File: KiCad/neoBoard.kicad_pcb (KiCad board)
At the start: 2 copper layers, 40 x 40 mm, 74 parts, among them J1 SW, J10 CONN_01X04_Straight, J11 CONN_01X04_Straight, J12 CONN_01X04_Straight, J13 CONN_01X04_Straight, J2 μUSB, J3 BATT, J6 CONN_01X12_Straight, J7 CONN_02X12_Straight, J8 CONN_01X04_Straight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

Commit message: PCB updated
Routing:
- net GND: track 137.4 -> 285.6 mm, vias 116 -> 108
- net /MOTEN: track 18.2 -> 24.9 mm, vias 2 -> 4
- net 3.3V: track 113.0 -> 110.4 mm, vias 7 -> 9
- net 5V: track 159.6 -> 157.9 mm
- net Net-(C5-Pad1): track 19.2 -> 17.8 mm
- net Net-(Q1-Pad1): track 4.76 -> 3.71 mm, vias 2 -> 0

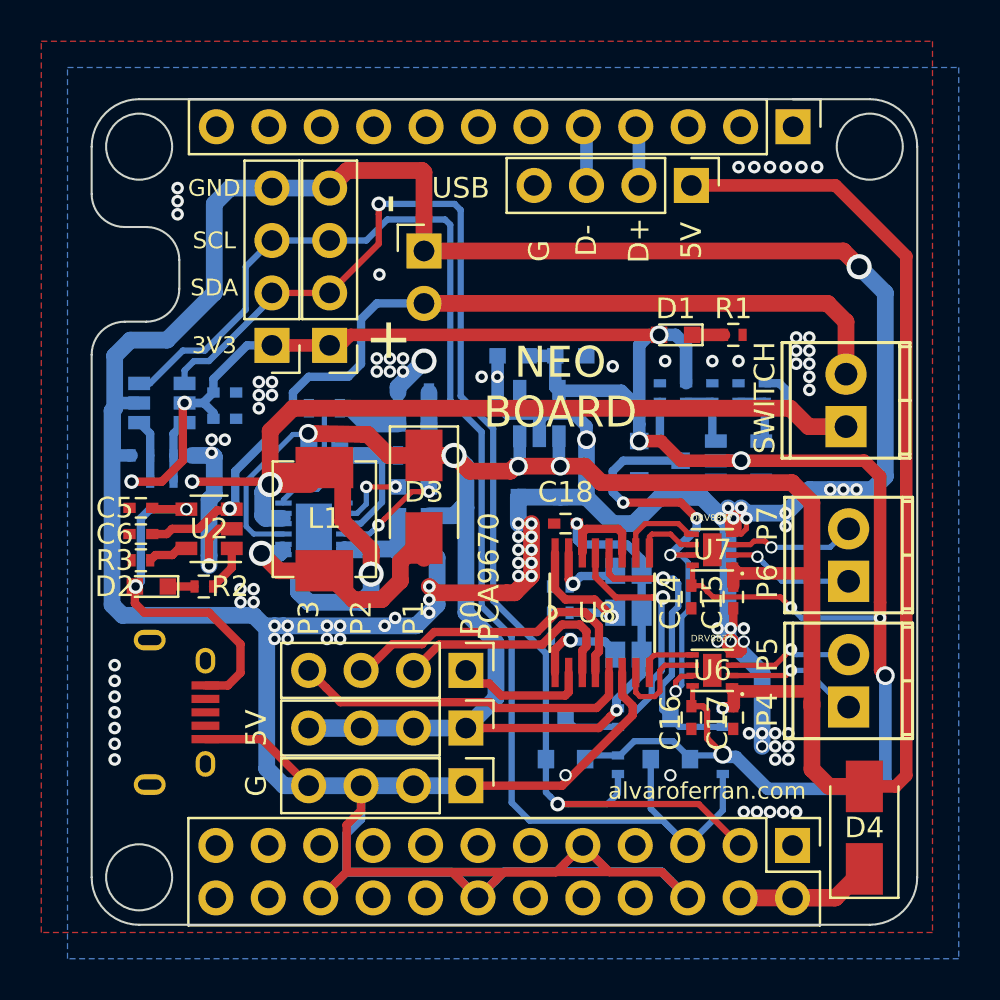
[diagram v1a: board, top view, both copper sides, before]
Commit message: Improved GND connections
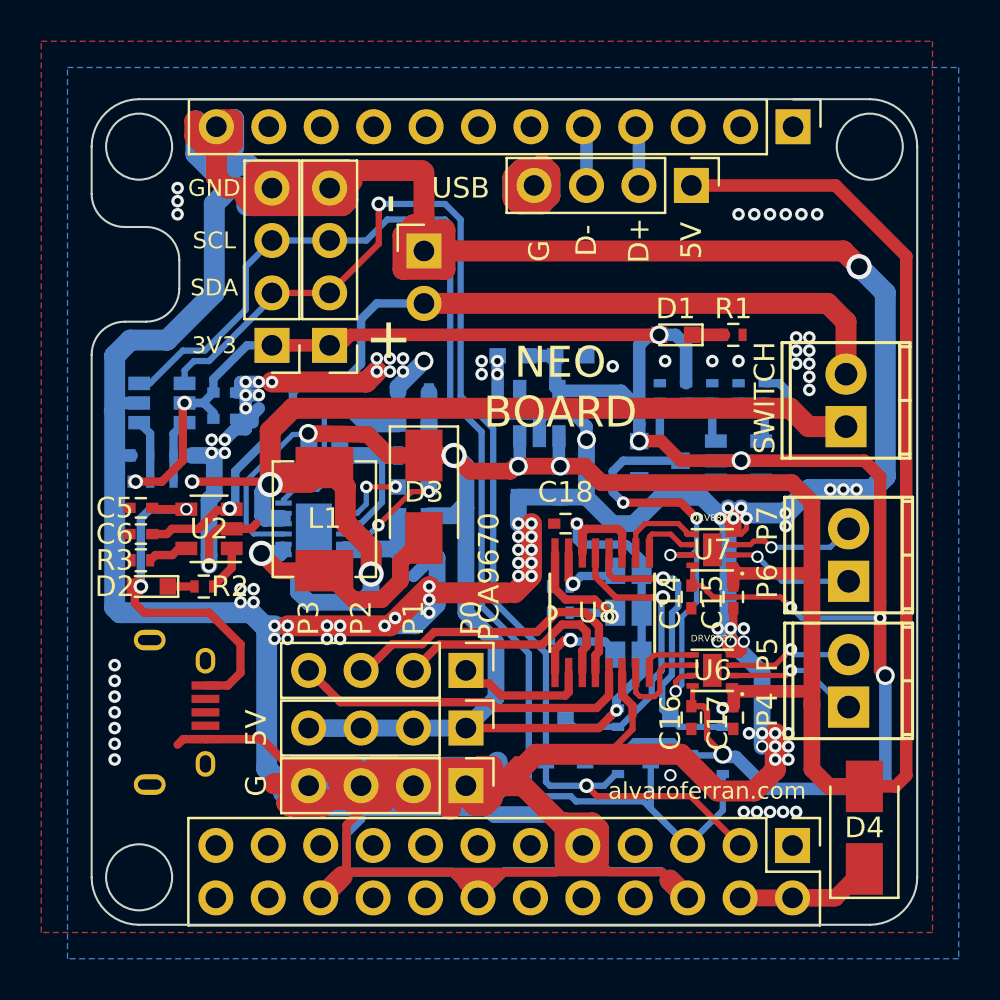
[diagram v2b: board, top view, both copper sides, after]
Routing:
- net GND: track 285.6 -> 502.5 mm, vias 108 -> 110
- net /SDA: track 63.6 -> 60.7 mm
- net Net-(D3-Pad2): track 13.2 -> 12.2 mm
- net /MOTEN: track 24.9 -> 25.8 mm
- net /SCL: track 67.4 -> 66.6 mm
- net VBAT: track 59.5 -> 60.2 mm
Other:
- net class Default: clearance 0 -> 0.0254
- rule trace_clearance: 0 -> 0.0254
- rule trace_min: 0.1524 -> 0.0254

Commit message: Change PCA9670 to PCA9685
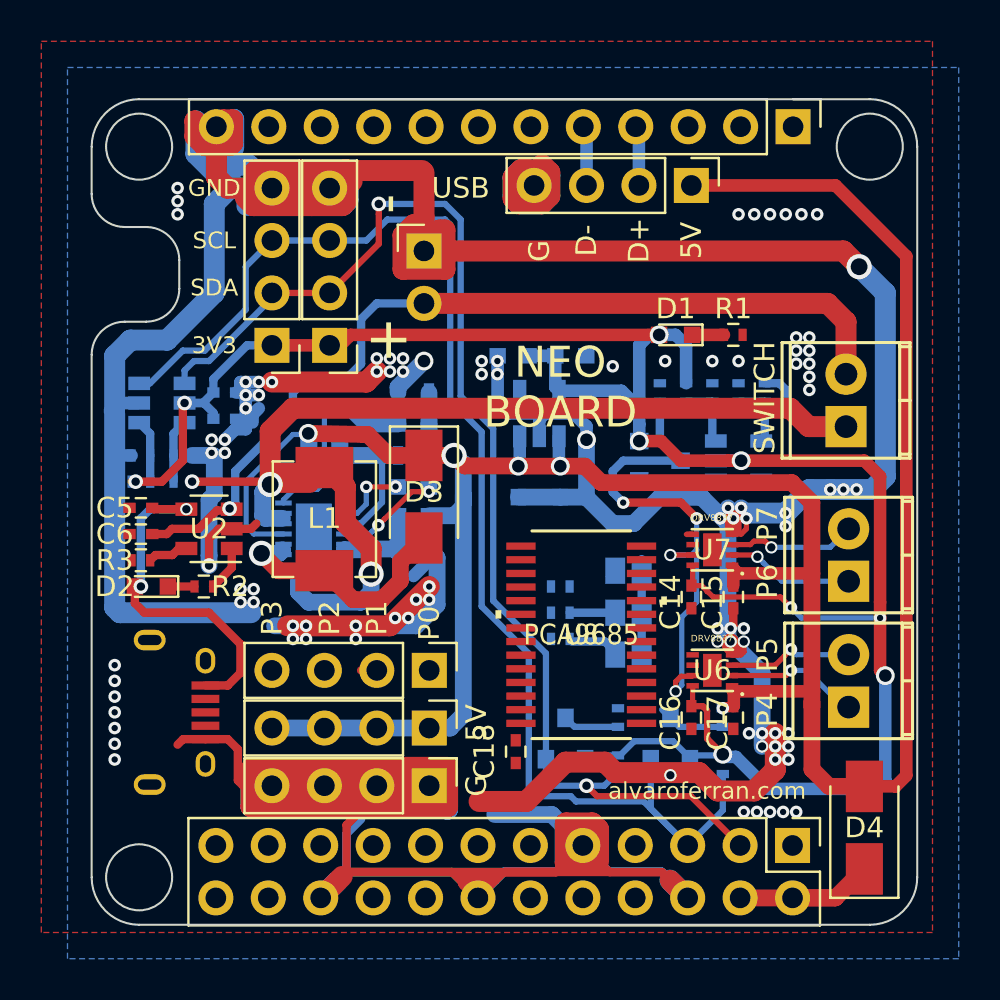
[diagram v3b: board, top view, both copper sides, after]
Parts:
- U8: value PCA9670 -> PCA9685; footprint alvaroferran:TSSOP-16 -> alvaroferran:TSSOP-28
- moved C18 11.3 mm to (169.0, 96.6), turned to 270 degrees
- moved J11 1.78 mm to (164.8, 98.3)
- moved J12 1.78 mm to (164.8, 95.5)
- moved J13 1.78 mm to (164.8, 92.7)
- moved U8 1.47 mm to (172.2, 91.0), turned to 180 degrees
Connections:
- U8 pad 1: Net-(JP3-Pad1) -> Net-(JP1-Pad1)
- U8 pad 10: /MOT2B -> /MOT1A
- U8 pad 11: 5V -> /MOT1B
- U8 pad 12: /SCLH -> /MOT2A
- U8 pad 13: /SDAH -> /MOT2B
- U8 pad 14: 5V -> GND
- U8 pad 15: Net-(JP1-Pad1) -> Net-(U8-Pad15)
- U8 pad 16: Net-(JP2-Pad1) -> Net-(U8-Pad16)
- U8 pad 2: /GPIO0 -> Net-(JP2-Pad1)
- U8 pad 3: /GPIO1 -> Net-(JP3-Pad1)
- U8 pad 4: /GPIO2 -> GND
- U8 pad 5: /GPIO3 -> GND
- U8 pad 6: GND -> /GPIO0
- U8 pad 7: /MOT1A -> /GPIO1
- U8 pad 8: /MOT1B -> /GPIO2
- U8 pad 9: /MOT2A -> /GPIO3
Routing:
- net GND: track 502.5 -> 443.6 mm, vias 110 -> 98
- net 5V: track 157.9 -> 134.7 mm, vias 7 -> 5
- net /GPIO3: track 16.7 -> 0.00 mm
- net /GPIO2: track 15.3 -> 0.00 mm
- net /SDAH: track 14.8 -> 2.82 mm, vias 1 -> 0
- net /GPIO1: track 11.5 -> 0.25 mm
- net /SCLH: track 14.3 -> 3.28 mm, vias 1 -> 0
- net /GPIO0: track 6.65 -> 0.00 mm
- net Net-(JP2-Pad1): track 7.15 -> 1.85 mm, vias 1 -> 0
- net /MOT1A: track 5.03 -> 0.00 mm
- net /MOT2B: track 4.43 -> 0.47 mm
- net Net-(JP1-Pad1): track 3.89 -> 0.36 mm, vias 1 -> 0
- net /MOT2A: track 3.15 -> 0.00 mm
- net /MOT1B: track 2.80 -> 0.00 mm
- net Net-(JP3-Pad1): track 4.58 -> 2.44 mm, vias 1 -> 0

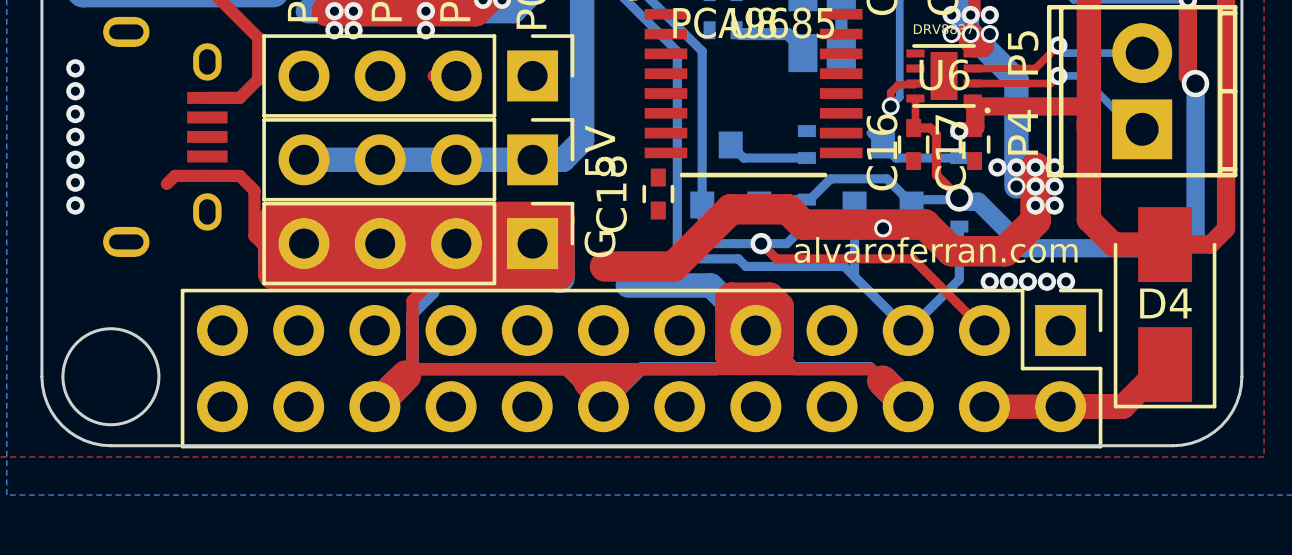
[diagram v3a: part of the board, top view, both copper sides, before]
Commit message: Improved GND connections
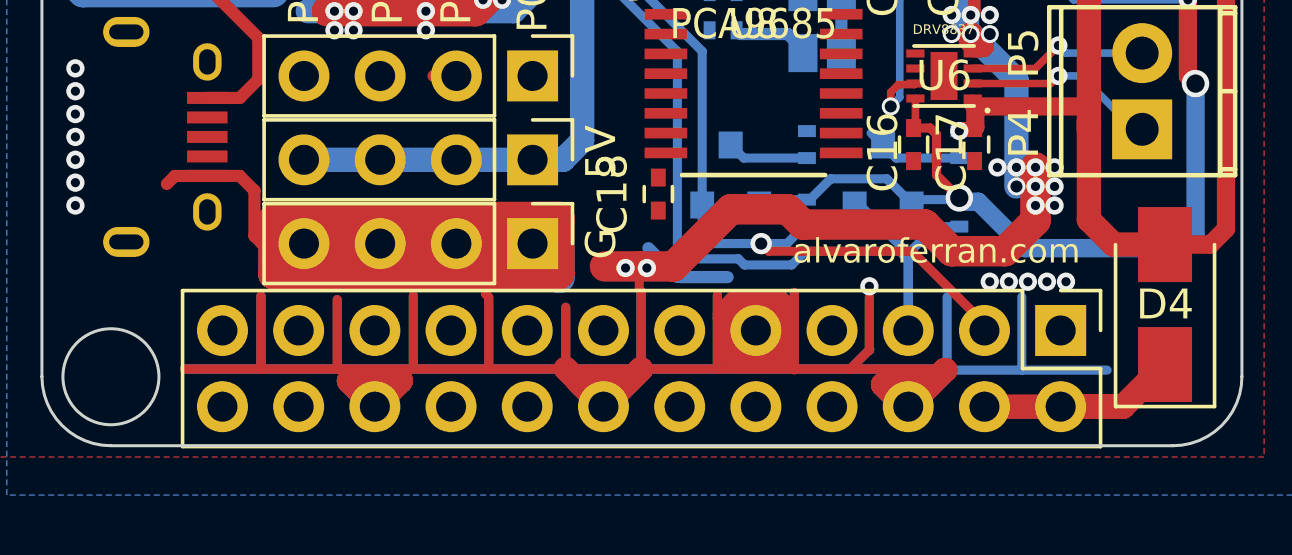
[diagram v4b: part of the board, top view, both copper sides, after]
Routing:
- net GND: track 443.6 -> 486.0 mm, vias 98 -> 100

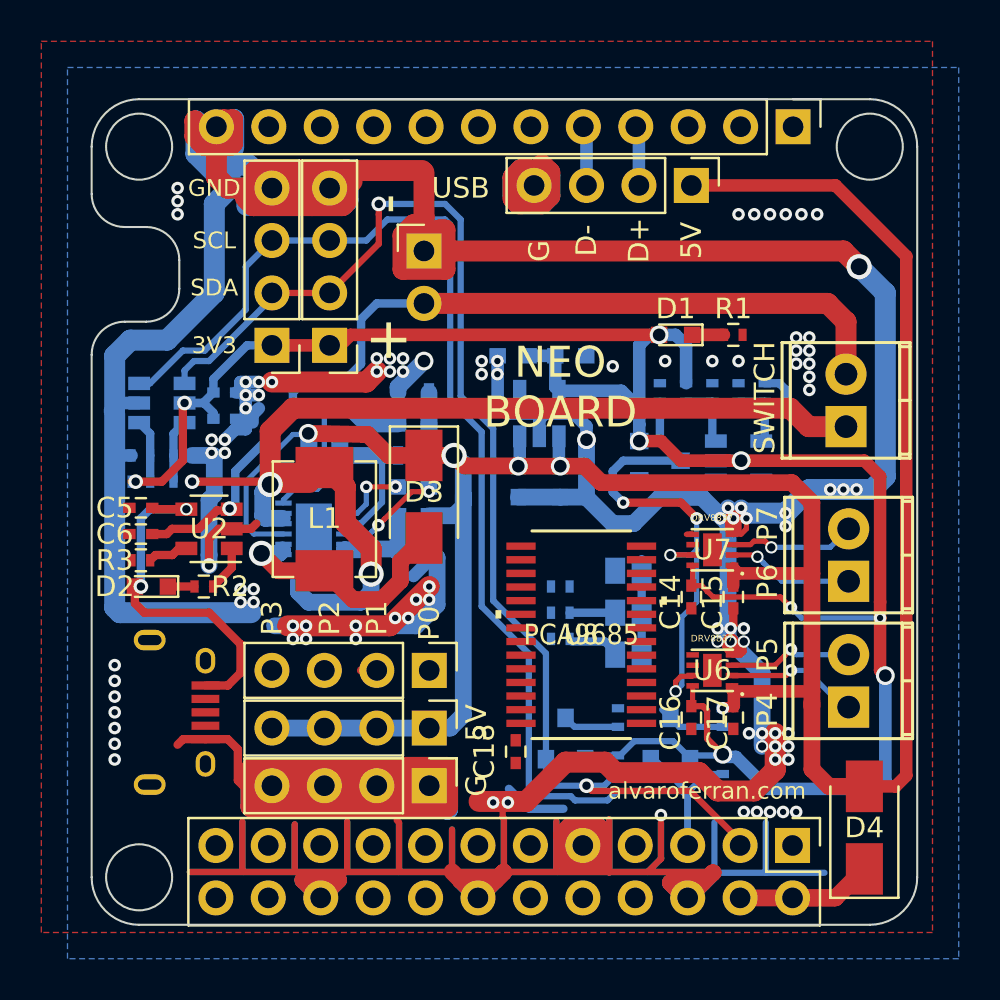
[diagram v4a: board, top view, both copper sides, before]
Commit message: Change PCA9670 to PCA9685
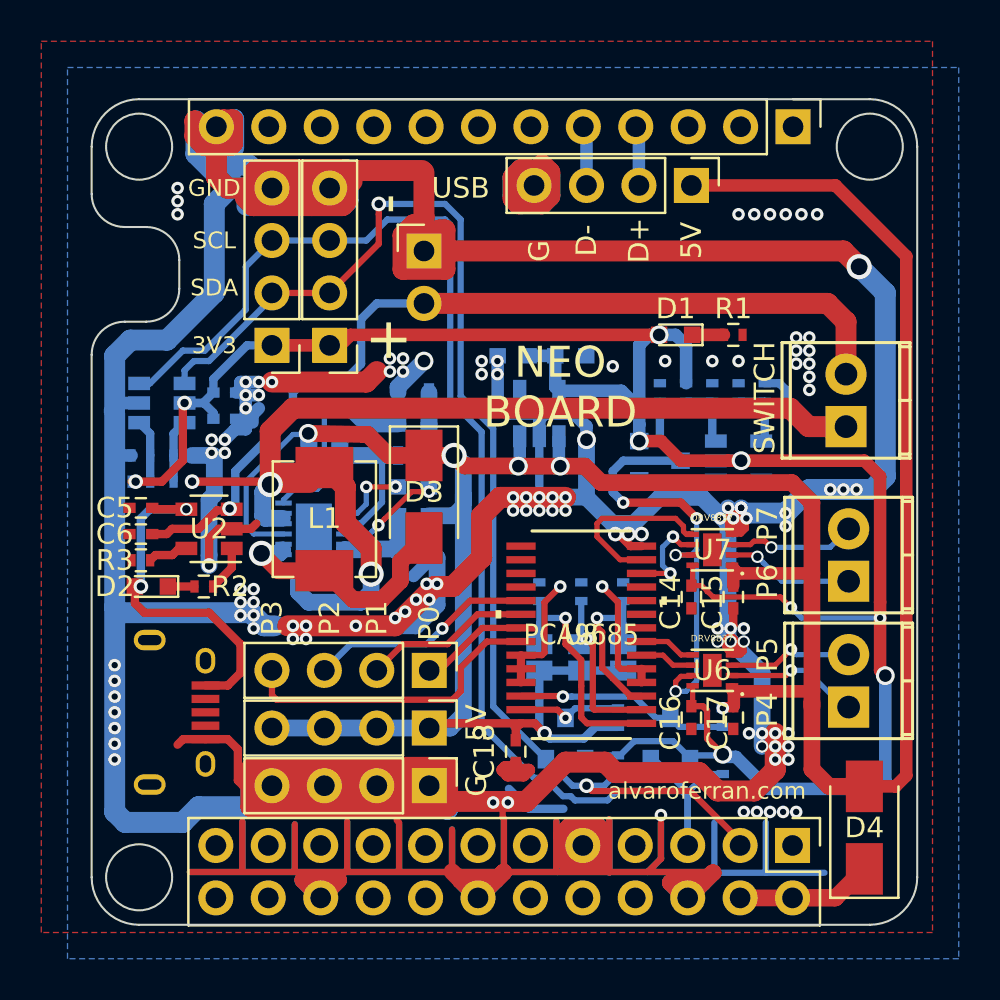
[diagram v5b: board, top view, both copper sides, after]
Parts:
- moved JP1 6.02 mm to (170.2, 92.1), turned to 180 degrees
- moved R20 3.81 mm to (174.2, 88.9), turned to 90 degrees
- moved JP2 3.15 mm to (172.2, 92.1), turned to 180 degrees
- moved R19 1.44 mm to (172.2, 88.9), turned to 90 degrees
- moved R18 1.05 mm to (170.2, 88.9), turned to 90 degrees
- moved JP3 0.29 mm to (174.2, 92.1), turned to 180 degrees
- turned R22 to 90 degrees
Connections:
- J2 pad 2: (no net) -> Net-(J2-Pad2)
- J2 pad 3: (no net) -> Net-(J2-Pad3)
- J2 pad 4: (no net) -> Net-(J2-Pad4)
- J6 pad 1: (no net) -> Net-(J6-Pad1)
- J6 pad 10: (no net) -> Net-(J6-Pad10)
- J6 pad 11: (no net) -> Net-(J6-Pad11)
- J6 pad 2: (no net) -> Net-(J6-Pad2)
- J6 pad 3: (no net) -> Net-(J6-Pad3)
- J6 pad 6: (no net) -> Net-(J6-Pad6)
- J6 pad 7: (no net) -> Net-(J6-Pad7)
- J6 pad 8: (no net) -> Net-(J6-Pad8)
- J6 pad 9: (no net) -> Net-(J6-Pad9)
- J7 pad 1: (no net) -> Net-(J7-Pad1)
- J7 pad 10: (no net) -> Net-(J7-Pad10)
- J7 pad 11: (no net) -> Net-(J7-Pad11)
- J7 pad 12: (no net) -> Net-(J7-Pad12)
- J7 pad 13: (no net) -> Net-(J7-Pad13)
- J7 pad 15: (no net) -> Net-(J7-Pad15)
- J7 pad 16: (no net) -> Net-(J7-Pad16)
- J7 pad 17: (no net) -> Net-(J7-Pad17)
- J7 pad 18: (no net) -> Net-(J7-Pad18)
- J7 pad 19: (no net) -> Net-(J7-Pad19)
- J7 pad 21: (no net) -> Net-(J7-Pad21)
- J7 pad 22: (no net) -> Net-(J7-Pad22)
- J7 pad 23: (no net) -> Net-(J7-Pad23)
- J7 pad 24: (no net) -> Net-(J7-Pad24)
- J7 pad 7: (no net) -> Net-(J7-Pad7)
- J7 pad 8: (no net) -> Net-(J7-Pad8)
- U1 pad 4: (no net) -> Net-(U1-Pad4)
- U3 pad 1: (no net) -> Net-(U3-Pad1)
- U8 pad 10: /MOT1A -> Net-(U8-Pad10)
- U8 pad 11: /MOT1B -> Net-(U8-Pad11)
- U8 pad 15: Net-(U8-Pad15) -> (no net)
- U8 pad 16: Net-(U8-Pad16) -> (no net)
- U8 pad 17: Net-(U8-Pad17) -> (no net)
- U8 pad 18: Net-(U8-Pad18) -> (no net)
- U8 pad 19: Net-(U8-Pad19) -> /GPIO2
- U8 pad 20: Net-(U8-Pad20) -> /GPIO1
- U8 pad 21: Net-(U8-Pad21) -> /GPIO0
- U8 pad 22: Net-(U8-Pad22) -> /GPIO3
- U8 pad 6: /GPIO0 -> /MOT1A
- U8 pad 7: /GPIO1 -> /MOT1B
- U8 pad 8: /GPIO2 -> Net-(U8-Pad8)
- U8 pad 9: /GPIO3 -> Net-(U8-Pad9)
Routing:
- net GND: track 486.0 -> 535.2 mm, vias 100 -> 117
- net /GPIO3: track 0.00 -> 15.2 mm
- net 5V: track 134.7 -> 148.1 mm, vias 5 -> 6
- net Net-(JP1-Pad1): track 0.36 -> 11.6 mm, vias 0 -> 1
- net /GPIO2: track 0.00 -> 10.9 mm, vias 0 -> 1
- net /MOT2B: track 0.47 -> 8.65 mm
- net /GPIO1: track 0.25 -> 8.11 mm
- net /SCLH: track 3.28 -> 10.4 mm, vias 0 -> 1
- net Net-(JP3-Pad1): track 2.44 -> 8.46 mm, vias 0 -> 1
- net Net-(JP2-Pad1): track 1.85 -> 7.81 mm, vias 0 -> 1
- net /GPIO0: track 0.00 -> 5.30 mm
- net /MOT2A: track 0.00 -> 4.65 mm, vias 0 -> 2
- net /MOT1B: track 0.00 -> 2.74 mm
- net /MOT1A: track 0.00 -> 2.68 mm
- net /SDAH: track 2.82 -> 5.06 mm, vias 0 -> 1
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
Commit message: Charger track changed from 16mil to 24mil
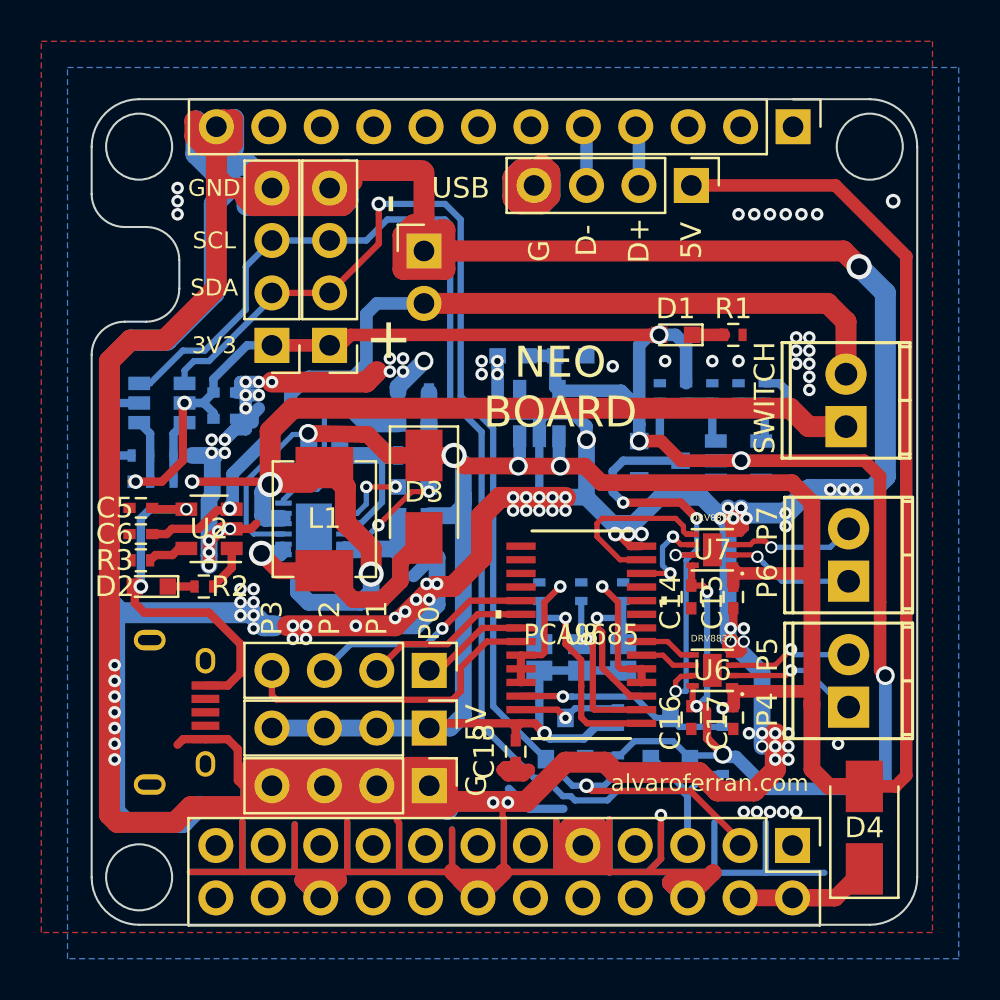
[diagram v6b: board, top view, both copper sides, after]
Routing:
- net GND: track 535.2 -> 575.0 mm, vias 117 -> 121
- net 3.3V: track 110.4 -> 108.3 mm
